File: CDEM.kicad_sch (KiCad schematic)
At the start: 31 parts, among them J1 USB_C_Receptacle_USB2.0, J2 6P6C, Q1 BSS138, SW1 BTN, SW2 RESET, U1 AMS1117-3.3, U2 USBLC6-2SC6, U3 CP2104, U4 ESP-12E

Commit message: finisched routing
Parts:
- removed Q1: BSS138, Package_TO_SOT_SMD:SOT-23, symbol Transistor_FET:BSS138
- added C9: 4.7uF, Capacitor_SMD:C_0603_1608Metric_Pad1.05x0.95mm_HandSolder, symbol Device:C_Small
- added Q1: 2N7002, Package_TO_SOT_SMD:SOT-23, symbol Transistor_FET:2N7002
- added Q2, Q3: S8050, Package_TO_SOT_SMD:SOT-23, symbol Drone_PCB-rescue:TRANS_NPN-MMBT2222AL-SparkFun-DiscreteSemi
- added R10, R11: 10k, Resistor_SMD:R_0603_1608Metric, symbol Device:R_Small
- added R12: 10k, Resistor_SMD:R_0603_1608Metric, symbol Device:R
- C1, C2, C3, C6: LCSC (none) -> C15850
- C4, C7, C8: LCSC (none) -> C14663
- C5: LCSC (none) -> C15849
- D1, D2: LCSC (none) -> C81598
- D3: LCSC (none) -> C72041
- D4: value Status -> COMM; LCSC (none) -> C72043
- D5: value Wifi -> DATA; LCSC (none) -> C72038
- J1: LCSC (none) -> C165948
- J2: LCSC (none) -> C305981
- R1, R2, R3, R6, R8, R9: LCSC (none) -> C25804
- R4, R5, R7: value R -> 1k; LCSC (none) -> C21190
- SW1, SW2: LCSC (none) -> C231329
- U1: LCSC (none) -> C6186
- U2: LCSC (none) -> C7519
- U3: LCSC (none) -> C47742
- U4: LCSC (none) -> C82898
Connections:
- net RX-LED is gone; now on net LED-DATA: D5.1 (K)
- net TX-LED is gone; now on net LED-COMM: D4.1 (K)
- net DATA: now also R2.2, U4.5 (GPIO14), Q1.3 (D); no longer U4.13 (MOSI)
- net GND: now also C9.2, Q1.2 (S)
- net GPIO0: now also Q2.3 (C)
- net RESET: now also Q3.3 (C)
- net SM-DATA: now also Q1.1 (G), R12.2
- net SM-DATA-REQ: now also U4.7 (GPIO13); no longer U4.12 (GPIO10)
- net VCC: now also R12.1
- net at U3.16 (VPP): now also C9.1
- net LED-COMM: now reaches U4.20 (GPIO5)
- net LED-DATA: now reaches U4.6 (GPIO12)
- new net: Q3.1 (B), R11.2
- new net: Q2.1 (B), R10.2
- new net DTR: Q2.2 (E), R11.1
- new net RTS: Q3.2 (E), R10.1
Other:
- moved on the sheet: R1

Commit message: finisching up the board
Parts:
- added J3: Conn_01x04, Connector_PinHeader_2.54mm:PinHeader_1x04_P2.54mm_Vertical, symbol Connector_Generic:Conn_01x04
- added L1: logo-devbit, cdem:logo_devbit_8mm, symbol cdem:logo-devbit
- added L2: logo-vives, cdem:logo_vives_10mm, symbol cdem:logo-vives
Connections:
- net +3V3: now also J3.1 (Pin_1)
- net GND: now also J3.4 (Pin_4)
- net USB-RX: now also J3.3 (Pin_3)
- net USB-TX: now also J3.2 (Pin_2)
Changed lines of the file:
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@@
+    (stroke (width 0) (type solid) (color 0 0 0 0))
+  )
+  (wire (pts (xy 245.11 101.6) (xy 255.27 101.6))
+    (stroke (width 0) (type solid) (color 0 0 0 0))
+  )
+  (wire (pts (xy 245.11 104.14) (xy 255.27 104.14))
     (stroke (width 0) (type solid) (color 0 0 0 0))
   )
@@
     (effects (font (size 1.27 1.27)) (justify left bottom))
   )
+  (label "USB-TX" (at 246.38 101.6 0)
+    (effects (font (size 1.27 1.27)) (justify left bottom))
+  )
+  (label "USB-RX" (at 246.38 104.14 0)
+    (effects (font (size 1.27 1.27)) (justify left bottom))
+  )
   (label "GPIO0" (at 256.54 125.73 180)
     (effects (font (size 1.27 1.27)) (justify right bottom))
@@
     (effects (font (size 1.27 1.27)) (justify left bottom))
   )
+  (symbol (lib_id "cdem:logo-devbit") (at 254 74.93 0) (unit 1)
+    (in_bom no) (on_board yes)
+    (property "Reference" "L1" (id 0) (at 254.635 73.7806 0)
+      (effects (font (size 1.27 1.27)) (justify left))
+    )
+    (property "Value" "logo-devbit" (id 1) (at 254.635 76.0793 0)
+      (effects (font (size 1.27 1.27)) (justify left))
+    )
+    (property "Footprint" "cdem:logo_devbit_8mm" (id 2) (at 254 74.93 0)
+      (effects (font (size 1.27 1.27)) hide)
+    )
+    (property "Datasheet" "" (id 3) (at 254 74.93 0)
+      (effects (font (size 1.27 1.27)) hide)
+    )
+  )
+  (symbol (lib_id "cdem:logo-vives") (at 254 80.01 0) (unit 1)
+    (in_bom no) (on_board yes)
+    (property "Reference" "L2" (id 0) (at 254.635 78.8606 0)
+      (effects (font (size 1.27 1.27)) (justify left))
+    )
+    (property "Value" "logo-vives" (id 1) (at 254.635 81.1593 0)
+      (effects (font (size 1.27 1.27)) (justify left))
+    )
+    (property "Footprint" "cdem:logo_vives_10mm" (id 2) (at 254 80.01 0)
+      (effects (font (size 1.27 1.27)) hide)
+    )
+    (property "Datasheet" "" (id 3) (at 254 80.01 0)
+      (effects (font (size 1.27 1.27)) hide)
+    )
+  )
   (symbol (lib_id "power:VBUS") (at 22.86 92.71 0) (unit 1)
     (in_bom yes) (on_board yes)
@@
     )
   )
+  (symbol (lib_id "power:+3V3") (at 255.27 99.06 0) (unit 1)
+    (in_bom yes) (on_board yes)
+    (property "Reference" "#PWR0106" (id 0) (at 255.27 102.87 0)
+      (effects (font (size 1.27 1.27)) hide)
+    )
+    (property "Value" "+3V3" (id 1) (at 255.6383 94.7356 0))
+    (property "Footprint" "" (id 2) (at 255.27 99.06 0)
+      (effects (font (size 1.27 1.27)) hide)
+    )
+    (property "Datasheet" "" (id 3) (at 255.27 99.06 0)
+      (effects (font (size 1.27 1.27)) hide)
+    )
+  )
   (symbol (lib_id "power:+3.3V") (at 262.89 24.13 0) (unit 1)
     (in_bom yes) (on_board yes)
@@
     )
     (property "Datasheet" "" (id 3) (at 240.03 45.72 0)
+      (effects (font (size 1.27 1.27)) hide)
+    )
+  )
+  (symbol (lib_id "power:GND") (at 255.27 106.68 0) (unit 1)
+    (in_bom yes) (on_board yes)
+    (property "Reference" "#PWR0105" (id 0) (at 255.27 113.03 0)
+      (effects (font (size 1.27 1.27)) hide)
+    )
+    (property "Value" "GND" (id 1) (at 255.397 111.0742 0))
+    (property "Footprint" "" (id 2) (at 255.27 106.68 0)
+      (effects (font (size 1.27 1.27)) hide)
+    )
+    (property "Datasheet" "" (id 3) (at 255.27 106.68 0)
       (effects (font (size 1.27 1.27)) hide)
     )
@@
     )
     (property "LCSC" "C2146" (id 4) (at 242.57 153.67 0)
+      (effects (font (size 1.27 1.27)) hide)
+    )
+  )
+  (symbol (lib_id "Connector_Generic:Conn_01x04") (at 260.35 101.6 0) (unit 1)
+    (in_bom yes) (on_board yes)
+    (property "Reference" "J3" (id 0) (at 262.3821 101.7714 0)
+      (effects (font (size 1.27 1.27)) (justify left))
+    )
+    (property "Value" "Conn_01x04" (id 1) (at 262.3821 104.0701 0)
+      (effects (font (size 1.27 1.27)) (justify left))
+    )
+    (property "Footprint" "Connector_PinHeader_2.54mm:PinHeader_1x04_P2.54mm_Vertical" (id 2) (at 260.35 101.6 0)
+      (effects (font (size 1.27 1.27)) hide)
+    )
+    (property "Datasheet" "~" (id 3) (at 260.35 101.6 0)
       (effects (font (size 1.27 1.27)) hide)
     )
@@
       (reference "#PWR0104") (unit 1) (value "VCC") (footprint "")
     )
+    (path "/ede1e51e-d970-4157-9fa5-9f82f666a53d"
+      (reference "#PWR0105") (unit 1) (value "GND") (footprint "")
+    )
+    (path "/ab6afbce-d660-4e65-8e74-c67e1a2297e7"
+      (reference "#PWR0106") (unit 1) (value "+3V3") (footprint "")
+    )
     (path "/a32d744a-8eea-4dc8-8484-5aee1a808196"
       (reference "C1") (unit 1) (value "10uF") (footprint "Capacitor_SMD:C_0805_2012Metric")
@@
       (reference "J2") (unit 1) (value "6P6C") (footprint "Connector_RJ:RJ12_Amphenol_54601")
     )
+    (path "/322d969e-d761-4c70-a8e9-8938482ff700"
+      (reference "J3") (unit 1) (value "Conn_01x04") (footprint "Connector_PinHeader_2.54mm:PinHeader_1x04_P2.54mm_Vertical")
+    )
+    (path "/623db2cc-58e4-412b-9b08-3e611c85074c"
+      (reference "L1") (unit 1) (value "logo-devbit") (footprint "cdem:logo_devbit_8mm")
+    )
+    (path "/d6f26c32-908f-49a9-a9c0-73cbb474a148"
+      (reference "L2") (unit 1) (value "logo-vives") (footprint "cdem:logo_vives_10mm")
+    )
     (path "/c2e61f06-4431-4cd4-bc30-0c5f2c1a0317"

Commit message: final version v4.0
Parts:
- added R13: 1M, Resistor_SMD:R_0603_1608Metric, symbol Device:R
- J3: now left out of the parts list
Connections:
- net DTR: now also U3.23 (DTR)
- net GND: now also R13.2
- net RTS: now also U3.19 (RTS)
- net SM-DATA: now also R13.1
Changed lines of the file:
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@@
+    (effects (font (size 1.27 1.27)) (justify left bottom))
+  )
+  (label "DTR" (at 165.1 148.59 0)
     (effects (font (size 1.27 1.27)) (justify left bottom))
   )
@@
   )
   (label "USB-RX" (at 165.1 158.75 0)
+    (effects (font (size 1.27 1.27)) (justify left bottom))
+  )
+  (label "RTS" (at 165.1 163.83 0)
     (effects (font (size 1.27 1.27)) (justify left bottom))
   )
@@
     )
   )
+  (symbol (lib_id "power:GND") (at 80.01 50.8 0) (unit 1)
+    (in_bom yes) (on_board yes)
+    (property "Reference" "#PWR0107" (id 0) (at 80.01 57.15 0)
+      (effects (font (size 1.27 1.27)) hide)
+    )
+    (property "Value" "GND" (id 1) (at 80.1243 55.1244 0))
+    (property "Footprint" "" (id 2) (at 80.01 50.8 0)
+      (effects (font (size 1.27 1.27)) hide)
+    )
+    (property "Datasheet" "" (id 3) (at 80.01 50.8 0)
+      (effects (font (size 1.27 1.27)) hide)
+    )
+  )
   (symbol (lib_id "power:GND") (at 82.55 187.96 0) (unit 1)
     (in_bom yes) (on_board yes)
@@
     )
     (property "LCSC" "C25804" (id 4) (at 80.01 30.48 0)
+      (effects (font (size 1.27 1.27)) hide)
+    )
+  )
+  (symbol (lib_id "Device:R") (at 80.01 46.99 0) (unit 1)
+    (in_bom yes) (on_board yes)
+    (property "Reference" "R13" (id 0) (at 81.788 45.8216 0)
+      (effects (font (size 1.27 1.27)) (justify left))
+    )
+    (property "Value" "1M" (id 1) (at 81.788 48.133 0)
+      (effects (font (size 1.27 1.27)) (justify left))
+    )
+    (property "Footprint" "Resistor_SMD:R_0603_1608Metric" (id 2) (at 78.232 46.99 90)
+      (effects (font (size 1.27 1.27)) hide)
+    )
+    (property "Datasheet" "~" (id 3) (at 80.01 46.99 0)
+      (effects (font (size 1.27 1.27)) hide)
+    )
+    (property "LCSC" "C17514" (id 4) (at 80.01 46.99 0)
       (effects (font (size 1.27 1.27)) hide)
     )
@@
   )
   (symbol (lib_id "Connector_Generic:Conn_01x04") (at 260.35 101.6 0) (unit 1)
-    (in_bom yes) (on_board yes)
+    (in_bom no) (on_board yes)
     (property "Reference" "J3" (id 0) (at 262.3821 101.7714 0)
       (effects (font (size 1.27 1.27)) (justify left))
@@
       (reference "#PWR0106") (unit 1) (value "+3V3") (footprint "")
     )
+    (path "/90707dec-766e-4181-a349-4ca77bba2793"
+      (reference "#PWR0107") (unit 1) (value "GND") (footprint "")
+    )
     (path "/a32d744a-8eea-4dc8-8484-5aee1a808196"
       (reference "C1") (unit 1) (value "10uF") (footprint "Capacitor_SMD:C_0805_2012Metric")
@@
       (reference "R12") (unit 1) (value "10k") (footprint "Resistor_SMD:R_0603_1608Metric")
     )
+    (path "/1f700cd5-8504-4615-9f82-e5ac1a7b71a0"
+      (reference "R13") (unit 1) (value "1M") (footprint "Resistor_SMD:R_0603_1608Metric")
+    )
     (path "/e0428c4e-266b-4dbe-8e5d-6b1fa7314fd8"

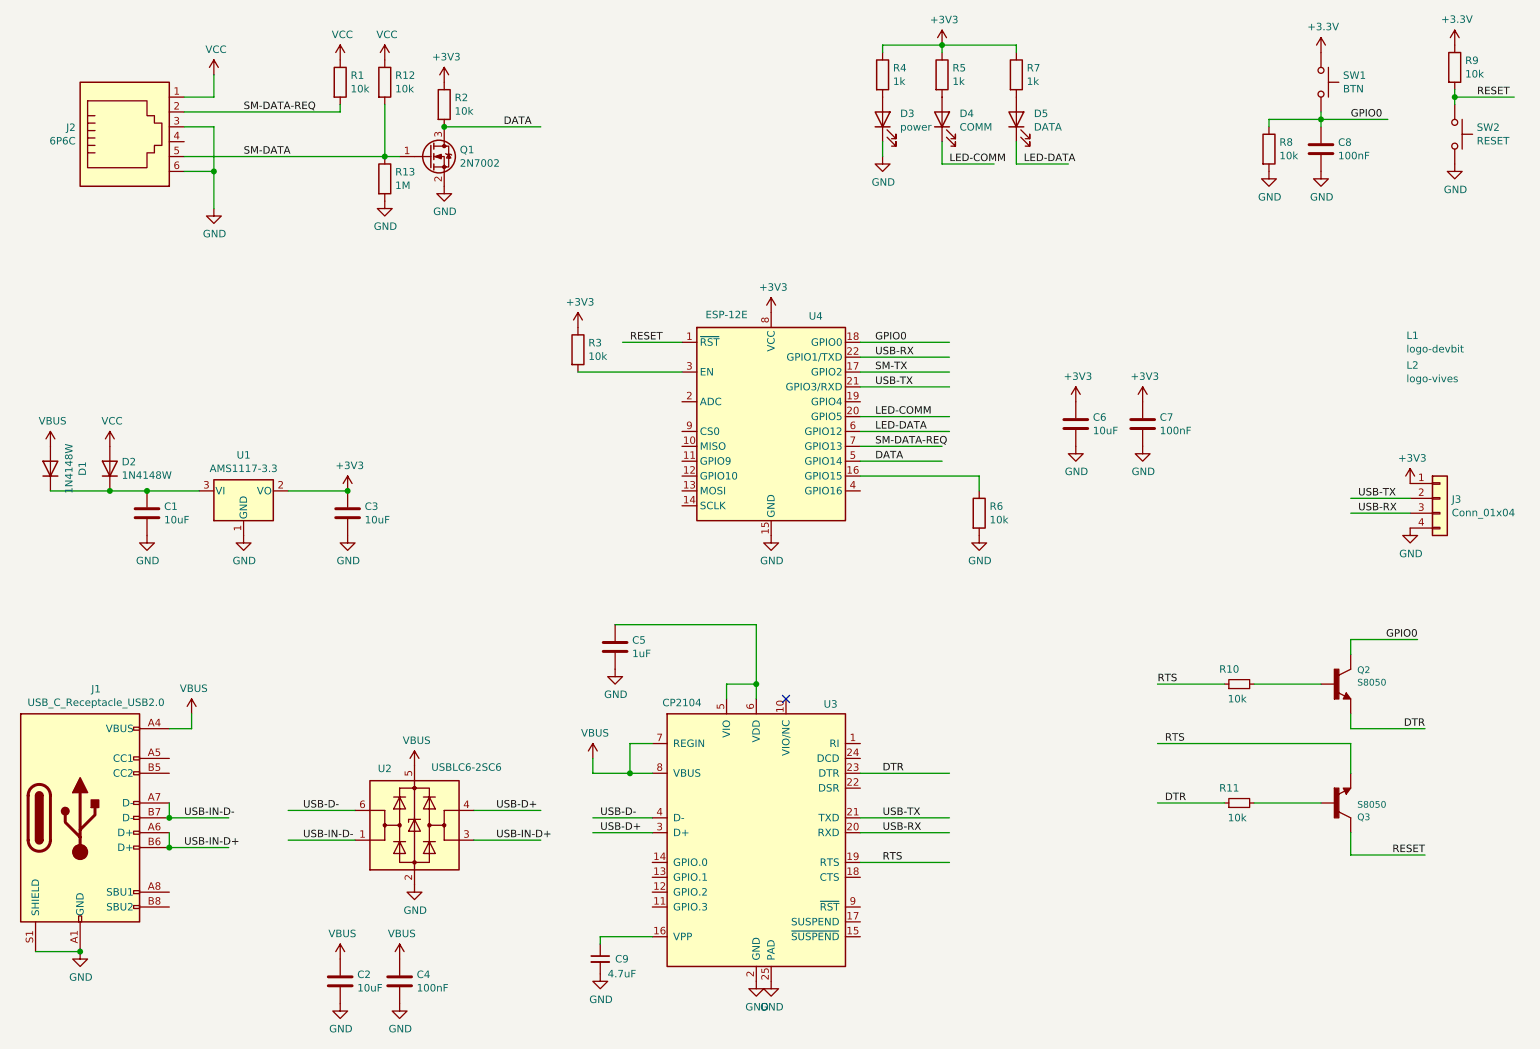
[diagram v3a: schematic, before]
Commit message: Replace LDO and diodes with better alternatives. Also add programming jumper
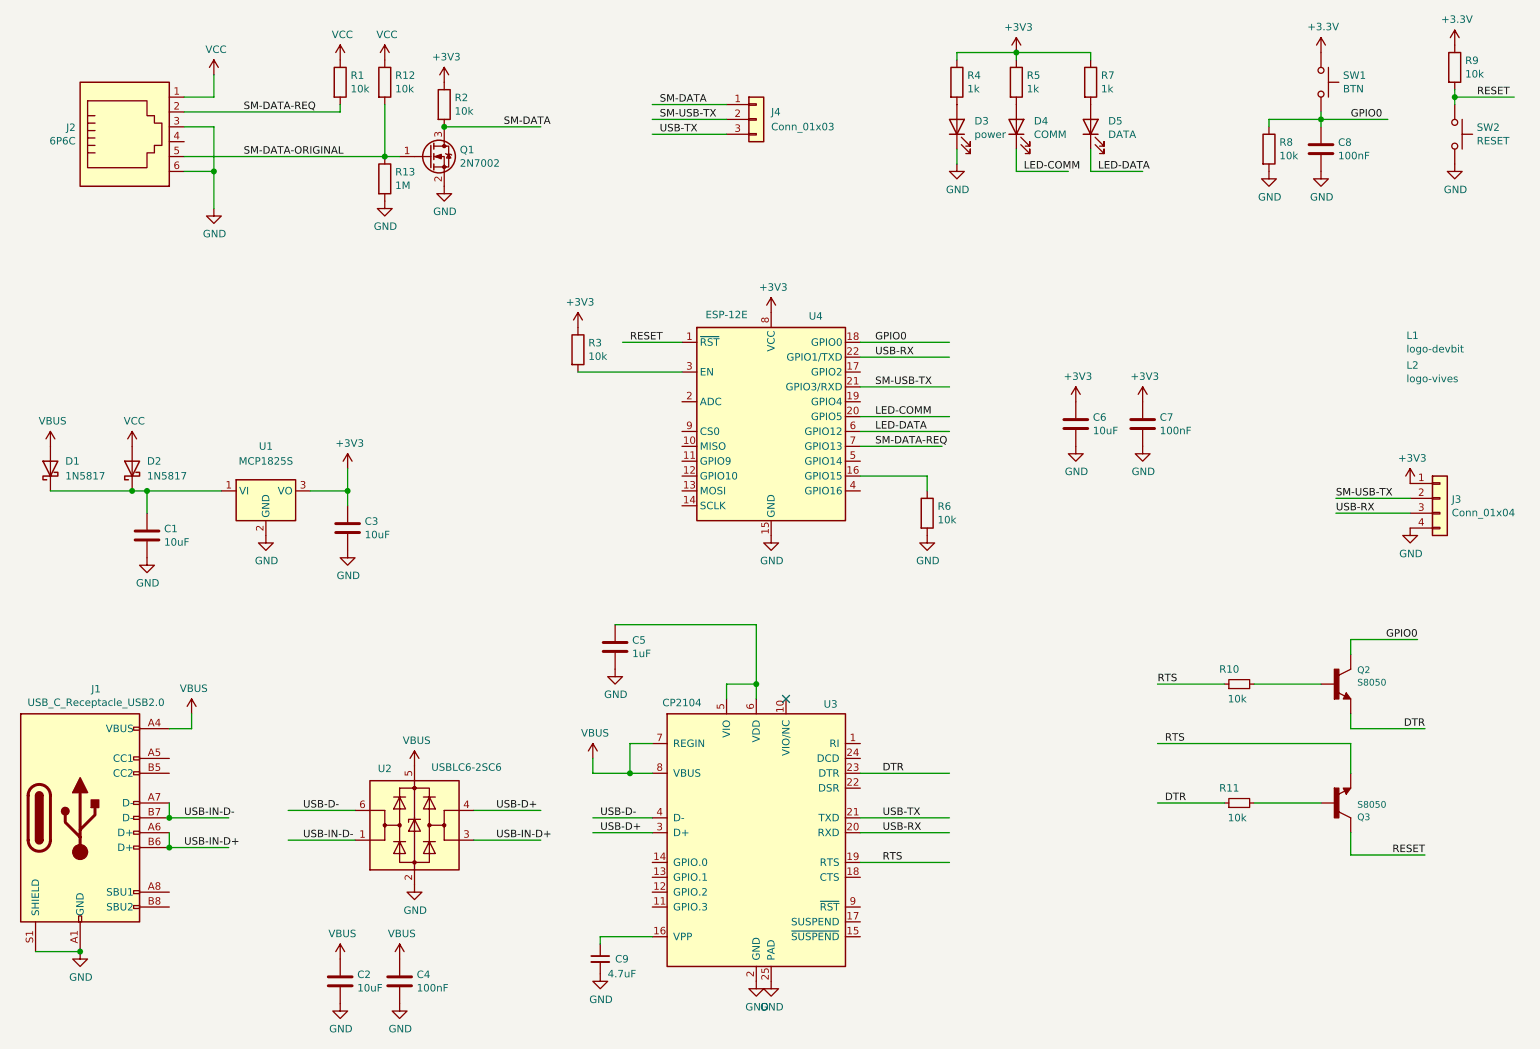
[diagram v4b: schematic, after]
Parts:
- removed D1, D2: 1N4148W, Diode_SMD:D_SOD-123, symbol Diode:1N4148W
- removed U1: AMS1117-3.3, Package_TO_SOT_SMD:SOT-223-3_TabPin2, symbol Regulator_Linear:AMS1117-3.3
- added D1, D2: 1N5817, Diode_SMD:D_SOD-123, symbol Diode:1N5817
- added J4: Conn_01x03, Connector_PinHeader_2.54mm:PinHeader_1x03_P2.54mm_Vertical, symbol Connector_Generic:Conn_01x03
- added U1: MCP1825S, Package_TO_SOT_SMD:SOT-223-3_TabPin2, symbol Regulator_Linear:MCP1825S
- C9: footprint Capacitor_SMD:C_0603_1608Metric_Pad1.05x0.95mm_HandSolder -> Capacitor_SMD:C_0805_2012Metric
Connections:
- net +3V3: now also U1.3 (VO)
- net GND: now also U1.2 (GND)
- net SM-DATA: now also Q1.3 (D), R2.2, J4.1 (Pin_1); no longer J2.5, Q1.1 (G), R12.2, R13.1
- net USB-TX: now also J4.3 (Pin_3); no longer J3.2 (Pin_2), U4.21 (GPIO3/RXD)
- net VBUS: now also D1.2 (A)
- net VCC: now also D2.2 (A)
- net at C1.1: now also D1.1 (K), D2.1 (K), U1.1 (VI)
- removed net DATA: Q1.3 (D), R2.2, U4.5 (GPIO14)
- net SM-TX: no longer names the net of U4.17 (GPIO2)
- new net SM-DATA-ORIGINAL: J2.5, Q1.1 (G), R12.2, R13.1
- new net SM-USB-TX: J3.2 (Pin_2), J4.2 (Pin_2), U4.21 (GPIO3/RXD)
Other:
- moved on the sheet: C1, C3, D3, D4, D5, R4, R5, R6, R7

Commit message: Finalize v5.0 and generate gerber and bom files
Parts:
- D1, D2: LCSC (none) -> C727113
- J4: LCSC (none) -> C390679
- U1: LCSC (none) -> C145411
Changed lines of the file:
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@@
+      (effects (font (size 1.27 1.27)) hide)
+    )
+    (property "LCSC" "C727113" (id 4) (at 22.86 96.52 90)
       (effects (font (size 1.27 1.27)) hide)
     )
@@
       (effects (font (size 1.27 1.27)) hide)
     )
+    (property "LCSC" "C727113" (id 4) (at 36.83 96.52 90)
+      (effects (font (size 1.27 1.27)) hide)
+    )
     (pin "1")
     (pin "2")
@@
     )
     (property "Datasheet" "~" (id 3) (at 143.51 36.83 0)
+      (effects (font (size 1.27 1.27)) hide)
+    )
+    (property "LCSC" "C390679" (id 4) (at 143.51 36.83 0)
       (effects (font (size 1.27 1.27)) hide)
     )
@@
       (effects (font (size 1.27 1.27)) hide)
     )
+    (property "LCSC" "C145411" (id 4) (at 59.69 100.33 0)
+      (effects (font (size 1.27 1.27)) hide)
+    )
